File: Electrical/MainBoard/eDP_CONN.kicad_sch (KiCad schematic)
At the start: 7 parts, among them J1 30_Pin_Zif

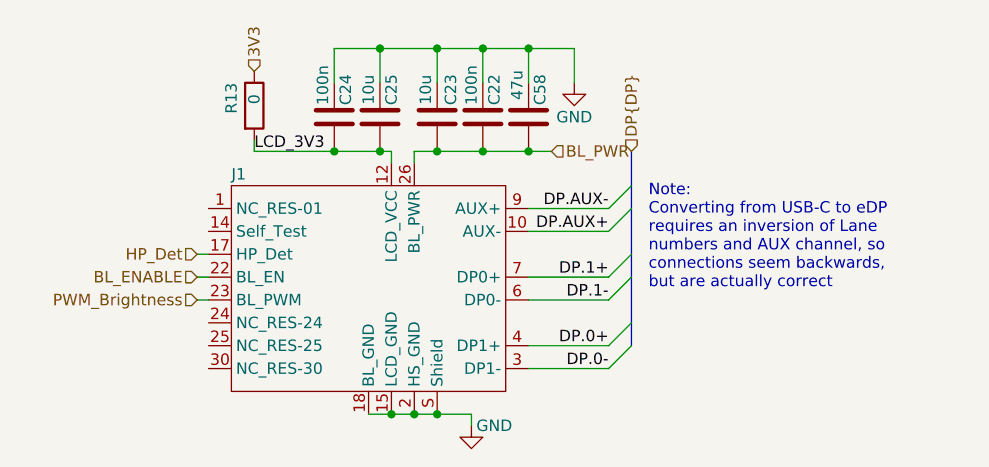
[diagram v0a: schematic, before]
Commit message: Added Mechanical components, fixed electrical err
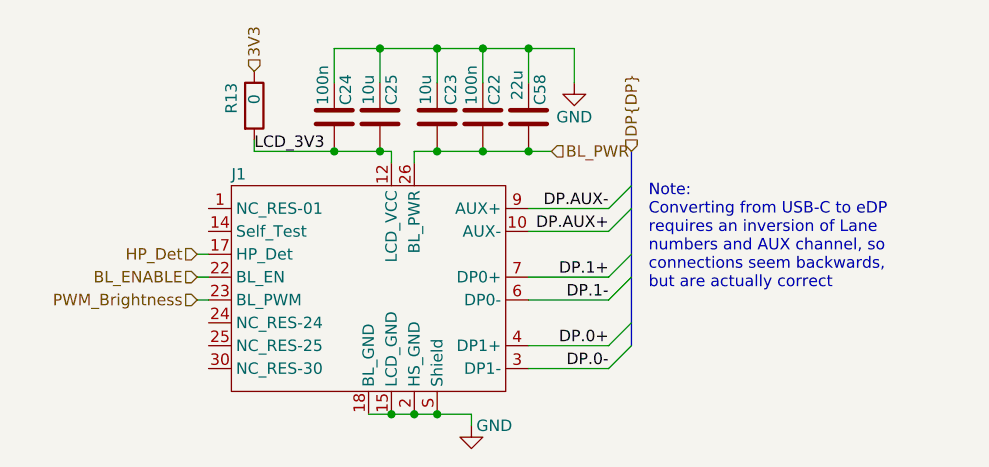
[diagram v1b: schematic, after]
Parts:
- C58: value 47u -> 22u
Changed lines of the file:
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@@
 			)
 		)
-		(property "Value" "47u"
+		(property "Value" "22u"
 			(at 153.67 29.464 90)
 			(effects
